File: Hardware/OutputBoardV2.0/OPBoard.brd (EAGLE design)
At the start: 47 x 78.4 mm, 20 parts, among them IC1 74AC08N, IC2 OP-AMP, IC3 OP-AMP, T1 BC547

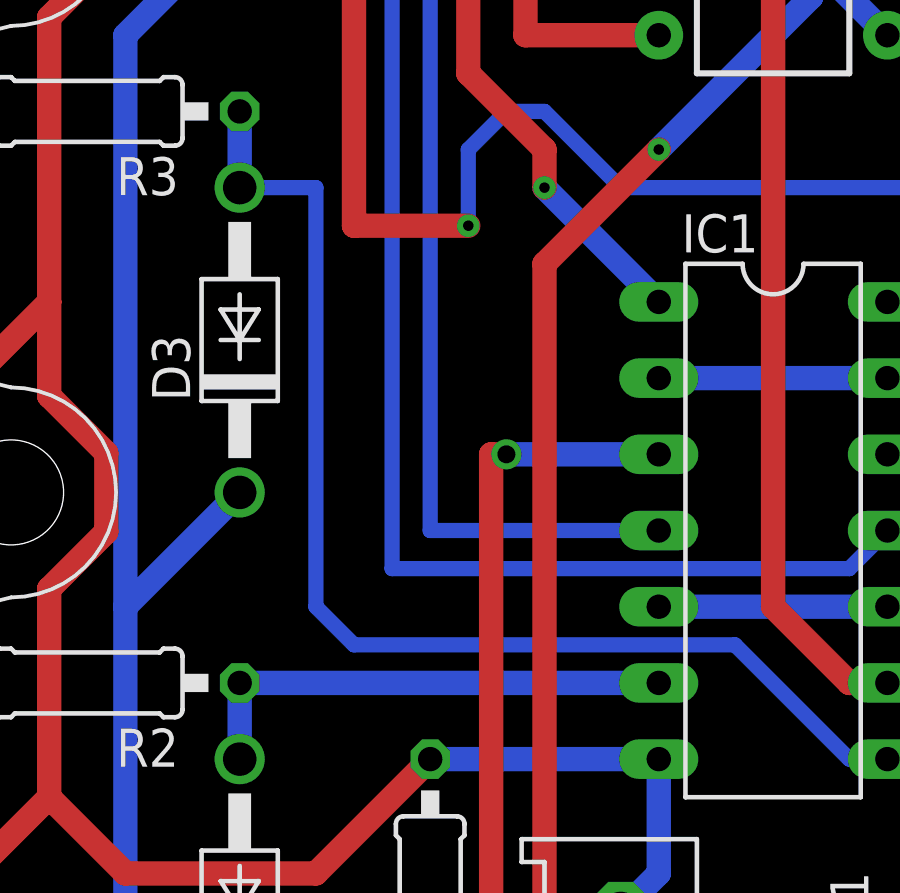
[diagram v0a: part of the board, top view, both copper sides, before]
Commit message: Letzte Änderungen an Netzteil, OP und IP Board
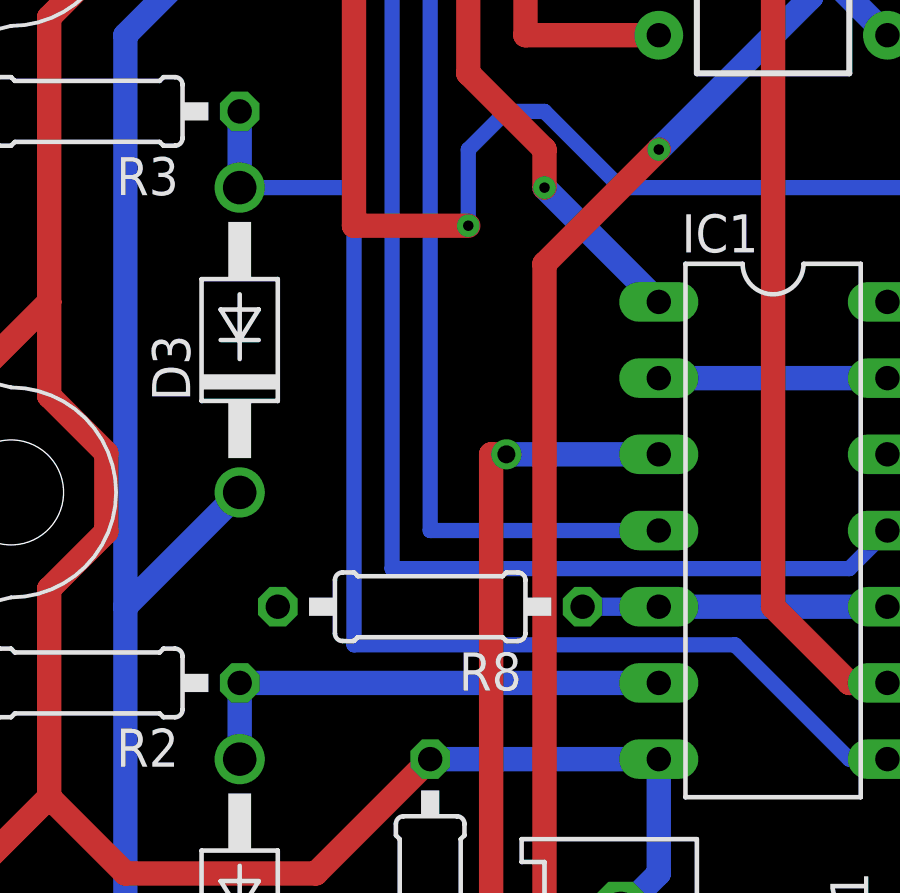
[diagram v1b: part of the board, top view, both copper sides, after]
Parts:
- added R8: 10k, rcl:0207/10
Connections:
- net ENABLE: now also R8.1
- net GND: now also R8.2
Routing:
- net ENABLE: track 90.5 -> 93.1 mm
- net N$7: track 40.2 -> 40.9 mm

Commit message: Minor Board Fixes
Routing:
- net LED: track 84.4 -> 81.2 mm
